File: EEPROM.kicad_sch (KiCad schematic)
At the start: 4 parts

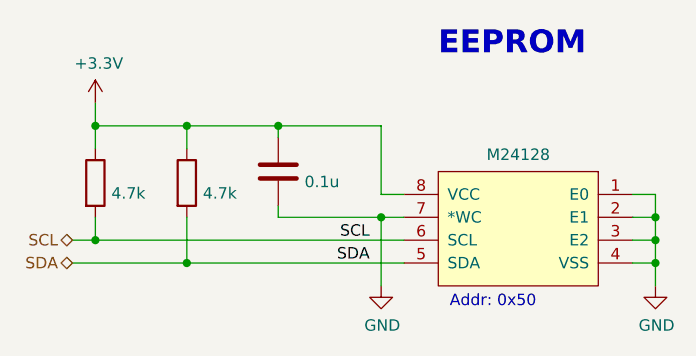
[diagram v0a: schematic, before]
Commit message: Update repo to only use one common library
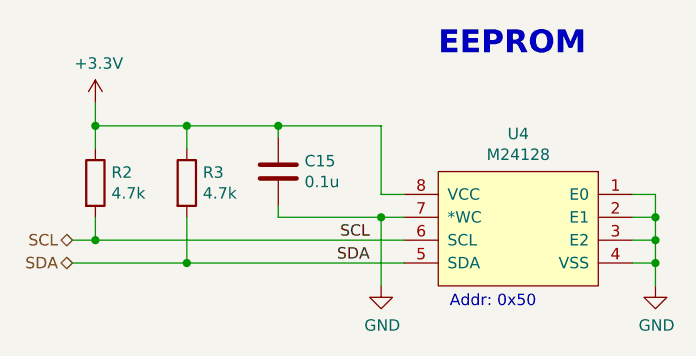
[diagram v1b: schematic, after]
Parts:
- gave numbers to parts that had none: 4
